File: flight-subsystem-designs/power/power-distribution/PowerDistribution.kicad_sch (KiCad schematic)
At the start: 144 parts, among them J1 Conn_02x26_Odd_Even, J11 Conn_01x04, J12 Conn_01x04, J13 Conn_01x04, J15 Conn_01x02, J2 Conn_02x26_Odd_Even, J3 Conn_01x02, J4 Conn_01x02, J5 Conn_01x02, J6 Conn_01x02, J7 Conn_01x02, J8 Conn_01x02, Q1 BC848ALT1G, Q2 IRLML2803PBFCT, Q3 IRLML2803PBFCT, Q4 NMOS, Q5 NMOS, U1 LT8610, U12 LTM8062AIV-PBF, U16 INA219AxD, U17 INA219AxD, U18 INA219AxD, U2 LT8610, U21 INA219AxD, U6 LT8610

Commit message: feat: pdu 4.0 in progress
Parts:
- removed R41: 0, Resistor_SMD:R_0603_1608Metric, symbol Device:R
- added U19: STM32L431CBTx, Package_QFP:LQFP-48_7x7mm_P0.5mm, symbol MCU_ST_STM32L4:STM32L431CBTx
- U14: renamed from U12; footprint PDU:LGA-77 -> LGA-77_15X9_2_LIT
- renumbered C15 to C1, C45 to C10, C47 to C11, C4 to C12, C7 to C13, C19 to C14, C1 to C15, C20 to C16, C8 to C17, C29 to C18, C13 to C19, C27 to C2, C17 to C20, C25 to C21, C5 to C22, C9 to C23, C21 to C24, C2 to C25, C10 to C26, C22 to C27, C30 to C28, C14 to C29, C42 to C3, C18 to C30, C26 to C31, C23 to C32, C6 to C33, C11 to C34, C3 to C35, C12 to C36, C24 to C37, C34 to C38, C35 to C39, C51 to C4, C33 to C5, C32 to C6, C31 to C7, C50 to C8, C46 to C9, D9 to D1, D1 to D10, D7 to D11, D11 to D12, D8 to D2, D10 to D3, D13 to D4, D4 to D5, D5 to D6, D6 to D7, D2 to D8, D3 to D9, J15 to J1, J13 to J10, J5 to J11, J8 to J12, J1 to J2, J6 to J5, J7 to J6, J2 to J7, J11 to J8, J12 to J9, L4 to L1, L1 to L2, L2 to L3, L3 to L4, Q4 to Q1, Q5 to Q2, Q1 to Q3, Q2 to Q4, Q3 to Q5, R15 to R1, R52 to R10, R43 to R11, R35 to R12, R37 to R13, R39 to R14, R2 to R15, R5 to R16, R7 to R17, R4 to R18, R6 to R19, R18 to R2, R9 to R20, R1 to R21, R3 to R22, R8 to R23, R10 to R24, R30 to R25, R14 to R26, R12 to R29, R33 to R3, R13 to R30, R11 to R31, R20 to R32, R19 to R33, R22 to R34, R23 to R35, R42 to R36, R21 to R37, R24 to R38, R29 to R39, R59 to R4, R25 to R40, R26 to R41, R34 to R42, R40 to R43, R31 to R44, R16 to R45, R17 to R46, R57 to R5, R32 to R6, R36 to R7, R38 to R8, R55 to R9, TP3 to TP1, TP1 to TP3, U4 to U1, U3 to U10, U9 to U11, U10 to U12, U5 to U13, U13 to U15, U11 to U16, U7 to U17, U8 to U18, U21 to U2, U17 to U3, U16 to U4, U18 to U5, U1 to U6, U2 to U7, U6 to U8, U14 to U9
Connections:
- net CHRG is gone; now on net ~{CHRG_STAT}: J2.24 (Pin_24)
- net FAULT is gone; now on net ~{CHRG_FAULT}: J2.22 (Pin_22)
- net VIN_REG is gone; now on net VINA: U14.L6 (VINREG)
- net GND: no longer U14.B4 (GND), U14.E1 (GND), U14.E2 (GND), U14.E3 (GND), U14.E4 (GND), U14.E5 (GND)
- net CHARGE_VIN: no longer names the net of C38.2, U14.K1 (VIN), U14.K2 (VIN), U14.K3 (VIN), U14.L1 (VIN), U14.L2 (VIN), U14.L3 (VIN)
- net SOLAR_PRE_MPPT renamed VINA
- net SOLAR_TMP_+Y: no longer names the net of J2.48 (Pin_48)
- net SOLAR_TMP_-Y: no longer names the net of J2.50 (Pin_50)
- net SOLAR_TMP_-Z: no longer names the net of J2.49 (Pin_49)
- new net: U19.23 (VSS), U19.35 (VSS), U19.47 (VSS)
- no-connect marks 68 -> 72
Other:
- note added: "Battery Power Switch (ADCS)"
- note added: "Magnetoresistive RAM"
- note added: "RBF Circuit"
- note added: "Regulated Power Switches"
- note removed: "Power Switches"
- note removed: "RBF Pins"
- note removed: "To Be Integrated into v4 (alongside USB charging)"
- moved on the sheet: C38, C39, D11, D12, J3, J4, J5, J6, L1, Q1, Q2, R1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

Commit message: updates from old computer
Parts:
- removed C20: 0.1uF, Capacitor_SMD:C_0603_1608Metric, symbol Device:C
- removed C30: 1uF, Capacitor_SMD:C_0603_1608Metric, symbol Device:C_Polarized
- removed D6: 150060AS75000, LED_SMD:LED_0603_1608Metric, symbol Device:LED
- removed J1, J5: Conn_01x02, Connector_Molex:Molex_Pico-Lock_205338-0002_1x02-1MP_P2.00mm_Horizontal, symbol Connector_Generic:Conn_01x02
- removed R27: 150, Resistor_SMD:R_0603_1608Metric, symbol Device:R
- removed R36: TBD, Resistor_SMD:R_0603_1608Metric, symbol Device:R
- removed R39: 50k, Resistor_SMD:R_0603_1608Metric, symbol Device:R
- removed U11: ~, Package_SO:SOIC-8_3.9x4.9mm_P1.27mm, symbol pdu:LTC1478
- removed U16: ~, Package_DFN_QFN:Texas_RGW0020A_VQFN-20-1EP_5x5mm_P0.65mm_EP3.15x3.15mm_ThermalVias, symbol pdu:TPS281C30
- added J1: Conn_02x07_Top_Bottom, Connector_Harwin:Harwin_LTek-Male_2x07_P2.00mm_Vertical_StrainRelief, symbol Connector_Generic:Conn_02x07_Top_Bottom
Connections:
- net GND_REF: no longer J2.10 (Pin_10), J2.11 (Pin_11), J2.12 (Pin_12), J2.9 (Pin_9)
- no-connect marks 72 -> 75
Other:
- note removed: "50k = 1A Limit"
- note removed: "Kapton Switch"
- note removed: "Low-Side"

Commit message: feat: PDU updates and laser driver v1.0.1
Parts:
- removed C1, C18, C19, C21: 0.1uF, Capacitor_SMD:C_0603_1608Metric, symbol Device:C
- removed C10, C11, C8, C9: 0.1UF, Capacitor_SMD:C_0603_1608Metric, symbol Device:C
- removed C12, C13, C14: 10nF, Capacitor_SMD:C_0603_1608Metric, symbol Device:C
- removed C15, C16, C17: 4.7uF, Capacitor_SMD:C_0603_1608Metric, symbol Device:C
- removed C2, C25, C26, C27: 0.1uF, Capacitor_SMD:C_0805_2012Metric, symbol Device:C
- removed C22, C24: 10pF, Capacitor_SMD:C_0805_2012Metric, symbol Device:C
- removed C23: 4.7pF, Capacitor_SMD:C_0805_2012Metric, symbol Device:C
- removed C28, C29, C31: 1uF, Capacitor_SMD:C_0603_1608Metric, symbol Device:C_Polarized
- removed C3: 22uF, Capacitor_SMD:C_0805_2012Metric, symbol Device:C
- removed C32, C33, C34, C4, C5, C6, C7: 1uF, Capacitor_SMD:C_0603_1608Metric, symbol Device:C
- removed C35, C36: 68uF, Capacitor_SMD:C_1206_3216Metric, symbol Device:C
- removed C37: 68uF, Capacitor_SMD:C_0805_2012Metric, symbol Device:C
- removed C38: 4.7uF, Capacitor_SMD:C_1206_3216Metric, symbol Device:C
- removed C39: 4.7uF, Capacitor_Tantalum_SMD:CP_EIA-3528-12_Kemet-T, symbol Device:C
- removed D1, D2, D3: PMEG10020ELRX, Diode_SMD:Nexperia_CFP3_SOD-123W, symbol Device:D_Schottky
- removed D10, D11, D12, D8, D9: 150060VS75000, LED_SMD:LED_0603_1608Metric, symbol Device:LED
- removed D4, D5, D7: 150060AS75000, LED_SMD:LED_0603_1608Metric, symbol Device:LED
- removed H1, H2, H3, H4: MountingHole, MountingHole:MountingHole_3.2mm_M3_Pad_TopBottom, symbol Mechanical:MountingHole_Pad_MP
- removed J1: Conn_02x07_Top_Bottom, Connector_Harwin:Harwin_LTek-Male_2x07_P2.00mm_Vertical_StrainRelief, symbol Connector_Generic:Conn_02x07_Top_Bottom
- removed J10, J8, J9: Conn_01x04, Connector_Molex:Molex_Pico-Lock_205338-0004_1x04-1MP_P2.00mm_Horizontal, symbol Connector_Generic:Conn_01x04
- removed J11, J12, J3, J4: Conn_01x02, Connector_Molex:Molex_Pico-Lock_205338-0002_1x02-1MP_P2.00mm_Horizontal, symbol Connector_Generic:Conn_01x02
- removed J2, J7: Conn_02x26_Odd_Even, Connector_PinHeader_2.54mm:PinHeader_2x26_P2.54mm_Vertical, symbol Connector_Generic:Conn_02x26_Odd_Even
- removed J6: Conn_01x02, symbol Connector_Generic:Conn_01x02
- removed L1: AIMC-0805-2N2S-T, Inductor_SMD:L_0805_2012Metric, symbol Device:L
- removed L2, L4: 10uH, Inductor_SMD:L_Coilcraft_XxL4040, symbol Device:L
- removed L3: 8.2uH, Inductor_SMD:L_Coilcraft_XxL4040, symbol Device:L
- removed Q1, Q2: NMOS, Package_TO_SOT_SMD:TSOT-23, symbol Simulation_SPICE:NMOS
- removed Q3: BC848ALT1G, Package_TO_SOT_SMD:SOT-23-3, symbol Transistor_BJT:2N3904
- removed Q4, Q5: IRLML2803PBFCT, Package_TO_SOT_SMD:SOT-23-3, symbol Transistor_FET:NDT3055L
- removed R1, R2: 1M, Resistor_SMD:R_0603_1608Metric, symbol Device:R
- removed R10, R11, R9: 40m, Resistor_SMD:R_2512_6332Metric, symbol Device:R
- removed R12, R13, R14, R4, R5, R6, R7, R8: 10, Resistor_SMD:R_0603_1608Metric, symbol Device:R
- removed R15, R16, R17: 110k, Resistor_SMD:R_0603_1608Metric, symbol Device:R
- removed R18, R20: 243k, Resistor_SMD:R_0805_2012Metric, symbol Device:R
- removed R19: 412k, Resistor_SMD:R_0805_2012Metric, symbol Device:R
- removed R21: 100k, Resistor_SMD:R_0603_1608Metric, symbol Device:R
- removed R22, R23, R24: 1M, Resistor_SMD:R_0805_2012Metric, symbol Device:R
- removed R25, R30: 65, Resistor_SMD:R_0603_1608Metric, symbol Device:R
- removed R26, R28, R29, R45, R46: 150, Resistor_SMD:R_0603_1608Metric, symbol Device:R
- removed R3: 10m, Resistor_SMD:R_2512_6332Metric, symbol Device:R
- removed R31: 150, Capacitor_SMD:C_1206_3216Metric, symbol Device:R
- removed R32, R33, R34, R35: 10k, Resistor_SMD:R_0805_2012Metric, symbol Device:R
- removed R37, R38: 4.7k, Resistor_SMD:R_0805_2012Metric, symbol Device:R
- removed R40, R41: 100k, Resistor_SMD:R_0805_2012Metric, symbol Device:R
- removed R42, R44: 549k, Resistor_SMD:R_0603_1608Metric, symbol Device:R
- removed R43: 459k, Resistor_SMD:R_0603_1608Metric, symbol Device:R
- removed TP1, TP2, TP3: ~, TestPoint:TestPoint_Keystone_5000-5004_Miniature, symbol Connector:TestPoint
- removed U1: ~, Package_SO:SOIC-8-1EP_3.9x4.9mm_P1.27mm_EP2.41x3.3mm, symbol pdu:TMP36FSZ
- removed U10, U12, U9: ~, Package_SO:SOIC-8_3.9x4.9mm_P1.27mm, symbol pdu:LTC1478
- removed U13: ~, Package_SO:SOIC-8_3.9x4.9mm_P1.27mm, symbol pdu:SI4835DDY
- removed U14: LTM8062AIV-PBF, LGA-77_15X9_2_LIT, symbol pdu:LTM8062AIV-PBF
- removed U15: ~, Package_DFN_QFN:DFN-8-1EP_6x5mm_P1.27mm_EP2x2mm, symbol pdu:MR25H256ACDF
- removed U17, U18: ~, Package_SO:TSOP-6_1.65x3.05mm_P0.95mm, symbol pdu:SI3407DV-T1-GE3
- removed U19: STM32L431CBTx, Package_QFP:LQFP-48_7x7mm_P0.5mm, symbol MCU_ST_STM32L4:STM32L431CBTx
- removed U2, U3, U4, U5: INA219AxD, Package_SO:SOIC-8_3.9x4.9mm_P1.27mm, symbol Sensor_Energy:INA219AxD
- removed U6, U7, U8: LT8610, Package_SO:MSOP-16-1EP_3x4.039mm_P0.5mm_EP1.651x2.845mm_ThermalVias, symbol Regulator_Switching:LT8610
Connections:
- no-connect marks 75 -> 0
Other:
- added sheet Charging (charging.kicad_sch)
- added sheet Connectors (connectors.kicad_sch)
- added sheet Control (control.kicad_sch)
- added sheet Deployment (deployment.kicad_sch)
- added sheet Regulators (regulators.kicad_sch)
- added sheet Sensors (sensors.kicad_sch)
- added sheet Switches (switches.kicad_sch)
- note removed: "+Y Panel"
- note removed: "-Y Panel"
- note removed: "-Z Panel"
- note removed: "1206"
- note removed: "2512 (3W)"
- note removed: "2512 (5W)"
- note removed: "2A max current per switch"
- note removed: "3V3 Regulator"
- note removed: "5V Regulator"
- note removed: "ALL PASSIVES ARE 0603 UNLESS OTHERWISE SPECIFIED"
- note removed: "ALL PASSIVES ARE 0805"
- note removed: "Antenna Deployment"
- note removed: "Batt Heat"
- note removed: "Battery Charging"
- note removed: "Battery Power Switch (ADCS)"
- note removed: "Beagleboard Peripherals Switch"
- note removed: "Current/Voltage Sensors"
- note removed: "EDFA Regulator"
- note removed: "EDFA Switch"
- note removed: "High-Side"
- note removed: "I2C Address: 0x40"
- note removed: "I2C Address: 0x42"
- note removed: "I2C Address: 0x43"
- note removed: "I2C Address: 0x48"
- note removed: "Inhibits"
- note removed: "Inner Bank"
- note removed: "Input Voltage Filtering"
- note removed: "Magnetoresistive RAM"
- note removed: "Misc Switch 1"
- note removed: "Mounting Holes"
- note removed: "Outer Bank"
- note removed: "PC104 Connector"
- note removed: "RBF Circuit"
- note removed: "Regulated Power Switches"
- note removed: "Solar Panel Inputs"
- note removed: "Temperature Sensor"
- note removed: "Voltage Regulators"
- note removed: "output in celsius"
- note removed: "reference: Artemis Kit PDU v02"
- note removed: "reference: PyCubed Mainboard v05"
- company: UChicago Space Program -> UChicago Space Program :: PULSE-A
- title: PULSE-A Power Distribution Unit (PDU) -> Power Control and Distribution Unit (PCDU)

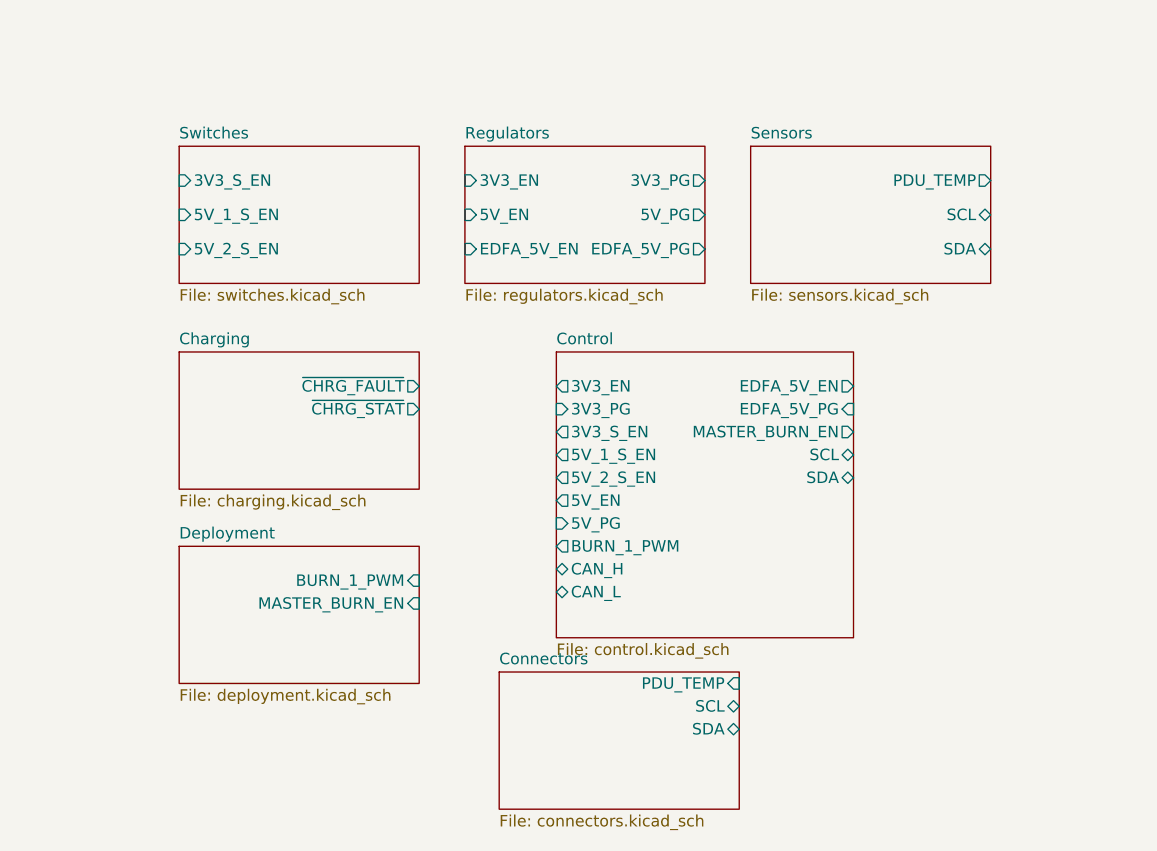
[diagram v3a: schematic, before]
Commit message: feat: PDU 4.0.0 (WIP)
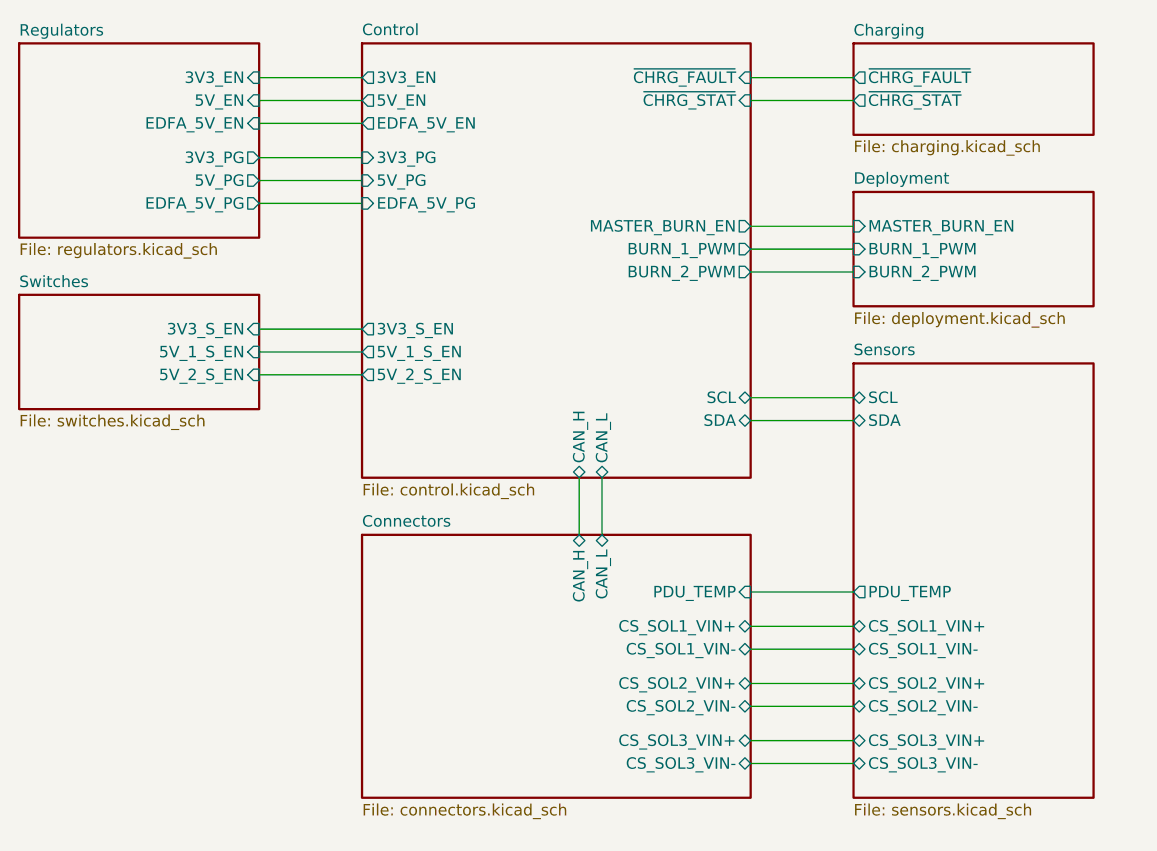
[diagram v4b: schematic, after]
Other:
- sheet Connectors ports: added CAN_H, CAN_L, CS_SOL1_VIN+, CS_SOL1_VIN-, CS_SOL2_VIN+, CS_SOL2_VIN-, CS_SOL3_VIN+, CS_SOL3_VIN-; removed SCL, SDA
- sheet Control ports: added BURN_2_PWM, ~{CHRG_FAULT}, ~{CHRG_STAT}; removed none
- sheet Deployment ports: added BURN_2_PWM; removed none
- sheet Sensors ports: added CS_SOL1_VIN+, CS_SOL1_VIN-, CS_SOL2_VIN+, CS_SOL2_VIN-, CS_SOL3_VIN+, CS_SOL3_VIN-; removed none

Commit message: shi
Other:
- sheet Charging ports: added VSOLAR_MPPT; removed none
- sheet Connectors ports: added BATT_CS, VSOLAR_MPPT; removed none
- sheet Sensors ports: added BATT_CS; removed none
